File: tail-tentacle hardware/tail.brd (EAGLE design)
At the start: 63.2 x 30.5 mm, 7 parts

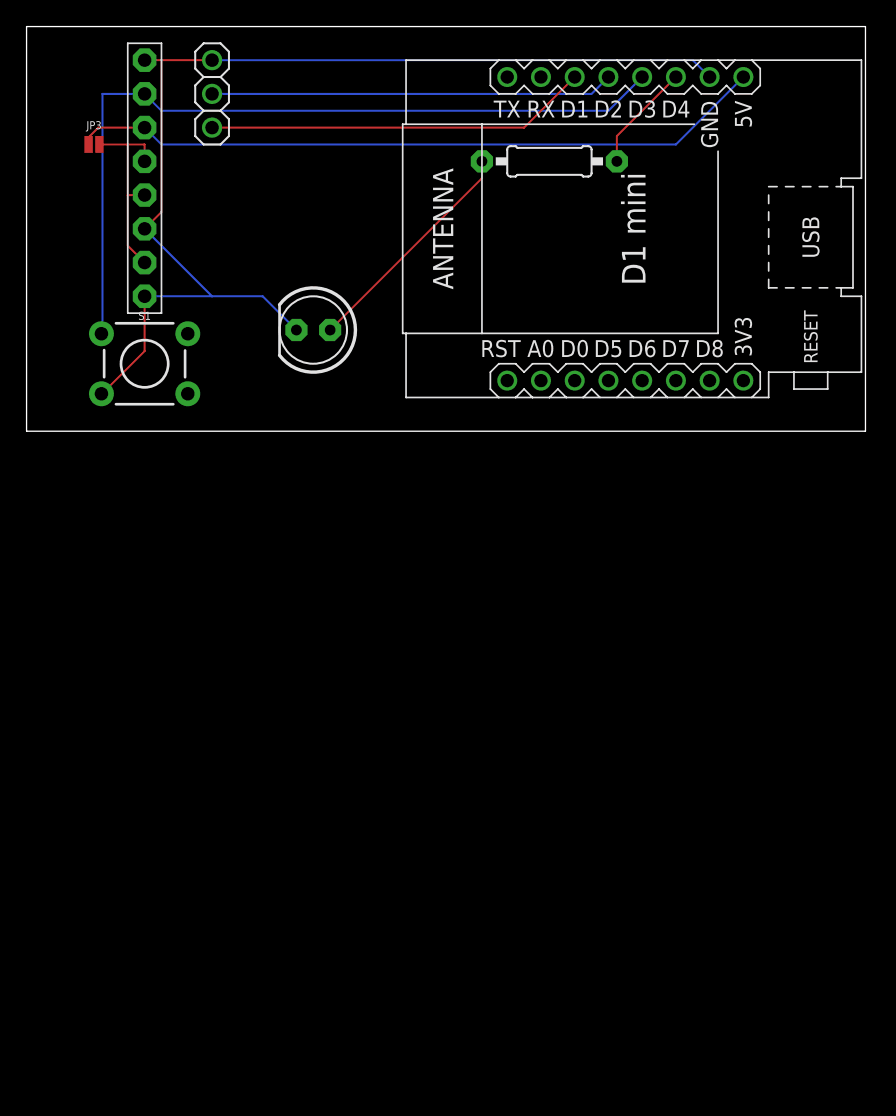
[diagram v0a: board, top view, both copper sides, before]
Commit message: Changed tail to tentacle
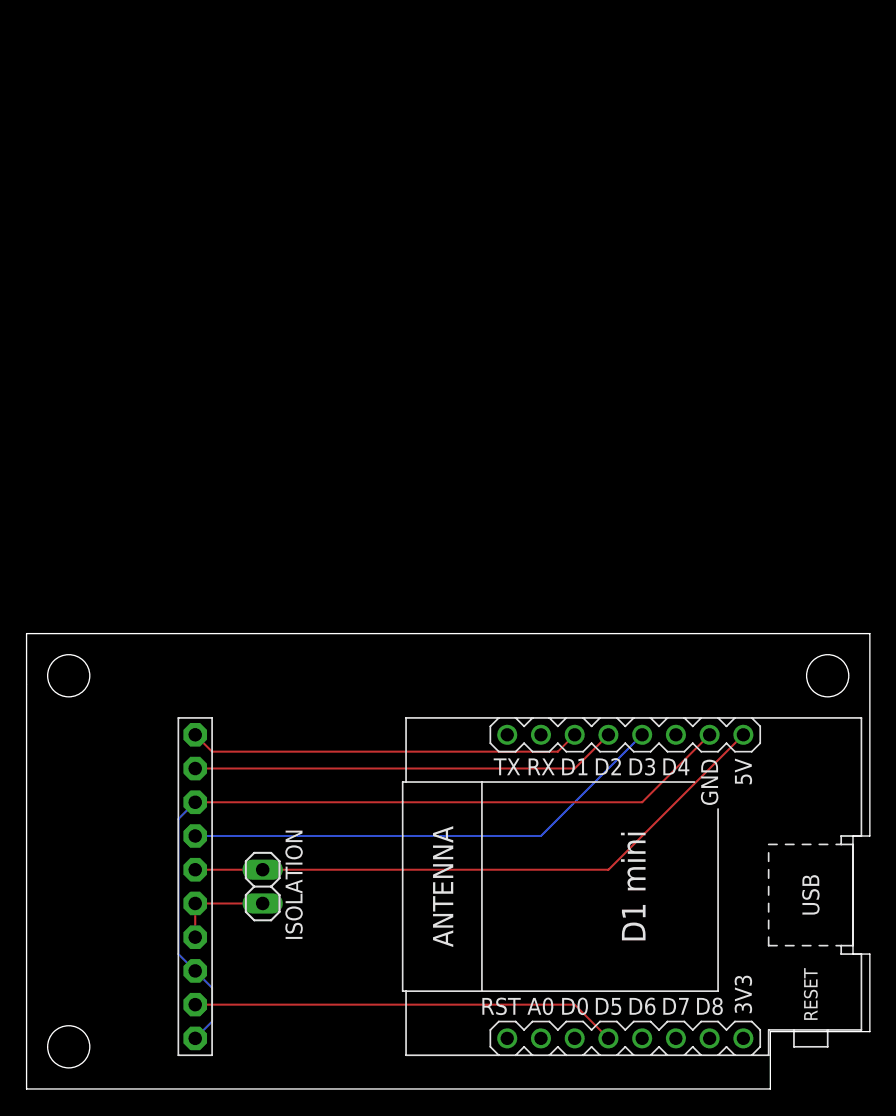
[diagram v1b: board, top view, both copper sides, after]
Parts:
- removed JP1: (no value), adafruit:1X08-BIG
- removed JP2: (no value), adafruit:1X03
- removed JP3: (no value), SparkFun-Jumpers:SMT-JUMPER_2_NC_PASTE_NO-SILK
- removed LED3: (no value), adafruit:LED5MM
- removed R4: 1K, adafruit:0207/10
- removed S1: MOMENTARY-SWITCH-SPST-PTH-6.0MM, SparkFun-Switches:TACTILE_SWITCH_PTH_6.0MM
- added ISOLATION: (no value), pinhead:1X02
- added U$1: PINHD-1X10, adafruit:1X10-BIG
- moved W1 49.5 mm to (45.7, 15.2)
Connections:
- removed net 0: JP1.1, JP1.3, JP1.8, JP2.1, LED3.K, S1.3, W1.JP2.7
- removed net N$10: JP1.7, S1.1, W1.JP2.5
- removed net N$9: LED3.A, R4.1
- new net N$1: U$1.7, W1.JP2.5
- new net N$7: U$1.2, W1.JP1.4
- net N$2: now also U$1.9; no longer JP2.2
- net N$3: now also U$1.10; no longer JP2.3
- net N$4: now also ISOLATION.1, U$1.4, U$1.5; no longer JP1.2, JP1.4, JP1.5, JP3.2
- net N$6: now also ISOLATION.2, U$1.6; no longer JP1.6, JP3.1
- net N$8: now also U$1.1, U$1.3, U$1.8, W1.JP2.7; no longer R4.2, W1.JP2.6
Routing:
- net 0: track 84.7 -> 0.00 mm
- net N$10: track 60.3 -> 0.00 mm
- net N$8: track 8.19 -> 60.7 mm
- net N$1: track 0.00 -> 36.8 mm
- net N$7: track 0.00 -> 32.2 mm
- net N$9: track 17.4 -> 0.00 mm
- net N$4: track 15.4 -> 7.62 mm
- net N$6: track 52.8 -> 45.5 mm
- net N$2: track 30.4 -> 32.2 mm
- net N$3: track 28.9 -> 29.6 mm
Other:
- board size 63.2 x 30.5 mm -> 63.5 x 34.3 mm
- board text added: "+5V in"
- board text added: "5V to ESP"
- board text added: "Button"
- board text added: "G"
- board text added: "H-BridgeA"
- board text added: "H-BridgeB"
- board text added: "Isolation"
- board text added: "LimitSW"
- board text removed: "D1 D2 G"
- board text removed: "G +5 G +5 JMP BTN"
- board text removed: "H-Bridge"
